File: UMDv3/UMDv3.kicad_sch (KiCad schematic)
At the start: 63 parts

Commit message: version 3.0 gerbers made
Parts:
- C101, C104, C108, C114, C115, C116, C117, C118, C119, C120, C121, C122, C123: value (none) -> 0.1uF/50V; footprint (none) -> db-smt:0603
- C102, C103, C107: value (none) -> 10uF/25V; footprint (none) -> db-smt:0805
- C105, C106: value (none) -> 2.2uF/16V; footprint (none) -> db-smt:0805
- C109, C110: value (none) -> 22pF/50V; footprint (none) -> db-smt:0603
- C111, C112, C113: value (none) -> 1uF/16V; footprint (none) -> db-smt:0805
- CON101, CON102: value (none) -> 10118192-0002LF; footprint (none) -> db-smt:USB-10118192-0002
- CON103, CON107: value (none) -> HDR1X3; footprint (none) -> db-thparts:HDR1X3
- CON104: value (none) -> JTAG-2X10-HDR; footprint (none) -> db-thparts:HDR2X10-JTAG-SHROUD
- CON105: value (none) -> 101-00405-75; footprint (none) -> db-smt:SDCARD-AMP-10100405
- CON106: value (none) -> UMDv3-CONN; footprint (none) -> db-thparts:UMDv3-CONN-DIP64-2
- D101, D102: value (none) -> LO_M67K-K2M1-24-Z; footprint (none) -> db-smt:SMD-2
- D103, D104: value (none) -> LG_M67K-G1J2-24-Z; footprint (none) -> db-smt:SMD-2
- FB101: value (none) -> 1K@100MHz; footprint (none) -> db-smt:0805
- MEC101, MEC102, MEC103, MEC104: value (none) -> NSP-4-6-01; footprint (none) -> db-thparts:4-40-SCREW
- R101: value (none) -> 1.5k; footprint (none) -> db-smt:0603
- R102, R103: value (none) -> 2.2k; footprint (none) -> db-smt:0603
- R104, R105, R106, R108, R110: value (none) -> 470; footprint (none) -> db-smt:0603
- R107, R111: value (none) -> 10k; footprint (none) -> db-smt:0603
- R109: value (none) -> 715; footprint (none) -> db-smt:0603
- SW101, SW102, SW103, SW104, SW105, SW106, SW107, SW108: value (none) -> PTS645SM43SMTR92_LFS; footprint (none) -> db-smt:PTS645
- U101: value (none) -> MCP23008T-E_SO; footprint (none) -> db-smt:SOIC-18
- U102: value (none) -> AZ1117CH-3.3TRG1; footprint (none) -> db-smt:SOT-223
- U103: value (none) -> STM32F407VET6TR; footprint (none) -> db-smt:TQFP-100
- U104: value (none) -> SSD1106-1.3-OLED-I2C; footprint (none) -> db-thparts:OLED-1.3-I2C
- X101: value (none) -> ABLS-8.000MHZ-B4-T; footprint (none) -> db-smt:HC-49US
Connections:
- no-connect marks 0 -> 1

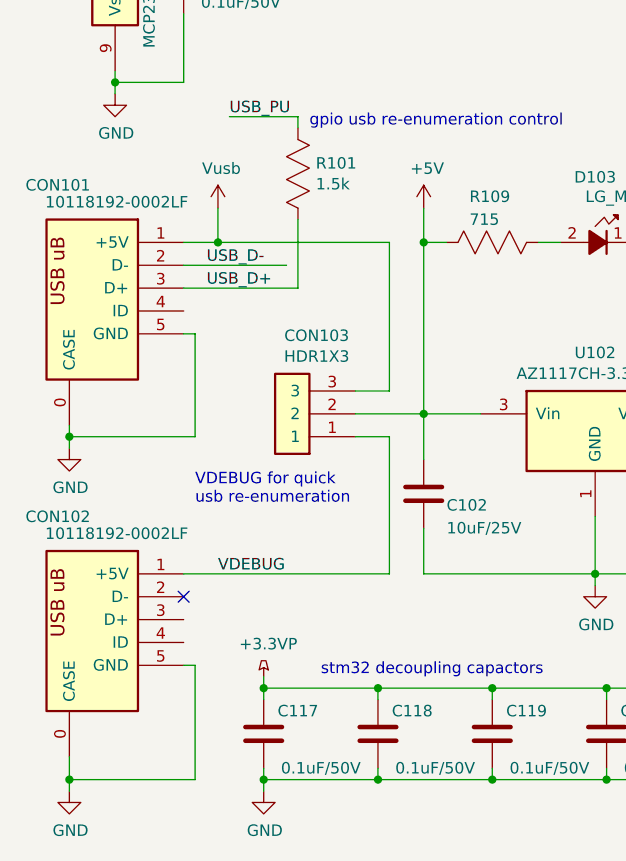
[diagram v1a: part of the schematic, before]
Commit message: updated sch for easier to solder usb conn, no pcb update yet
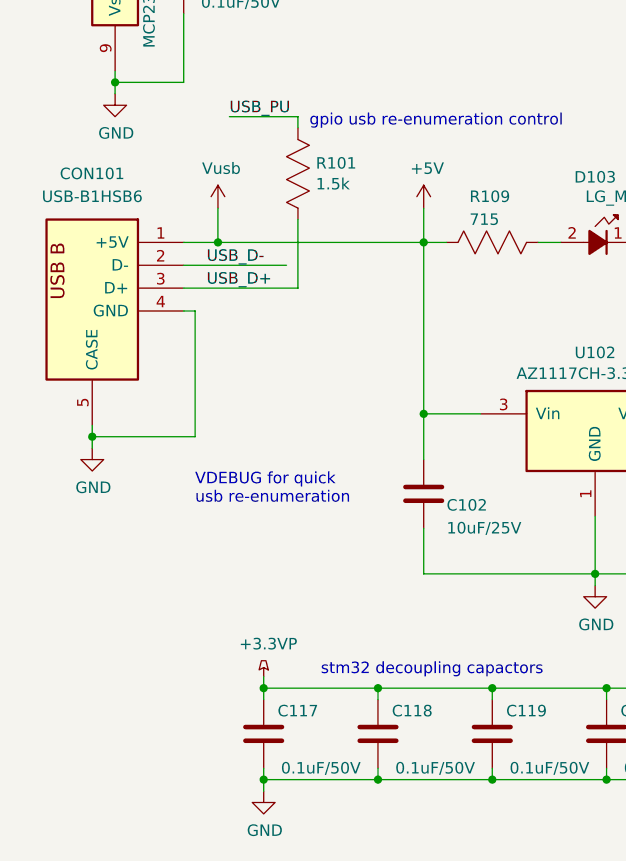
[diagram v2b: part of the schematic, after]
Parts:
- removed CON101, CON102: 10118192-0002LF, db-smt:USB-10118192-0002, symbol db-connectors:10118192-0002LF
- removed CON103: HDR1X3, db-thparts:HDR1X3, symbol db-connectors:HDR1X3
- added CON101: USB-B1HSB6, db-thparts:USB-B1HSxx, symbol db-connectors:USB-B1HSB6
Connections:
- net +5V: now also CON101.1 (+5V)
- net GND: now also CON101.4 (GND), CON101.5 (CASE)
- net USB_D+: now also CON101.3 (D+)
- net USB_D-: now also CON101.2 (D-)
- no-connect marks 1 -> 0

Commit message: work
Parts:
- removed U101: MCP23008T-E_SO, db-smt:SOIC-18, symbol db-sem:MCP23008T-E_SO
- added TP101: TP_2.25x3_ROUNDED, db-smt:TP_2.25x3_RND, symbol db-connectors:TP_2.25x3_ROUNDED
- added U101: MCP23008T-E_SS, db-smt:SSOP-20, symbol db-sem:MCP23008T-E_SS
- added logo101: db-logo, db-artwork:db-logo_10mm, symbol db-artwork:logo
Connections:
- net +3V3: now also U101.20 (Vdd), U101.3 (A2), U101.4 (A1), U101.5 (A0), U101.6 (~{RESET})
- net BACK: now also U101.17 (GP5)
- net DOWN: now also U101.13 (GP1)
- net GND: now also TP101.1, U101.9 (Vss)
- net LEFT: now also U101.12 (GP0)
- net MCP_INT: now also U101.8 (INT)
- net OK: now also U101.16 (GP4)
- net RIGHT: now also U101.15 (GP3)
- net SCL: now also U101.1 (SCL)
- net SDA: now also U101.2 (SDA)
- net UP: now also U101.14 (GP2)
- net at R105.2: now also U101.18 (GP6)
- net at R106.1: now also U101.19 (GP7)
- no-connect marks 0 -> 2
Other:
- note added: "i2c addr 0x27"
- note removed: "VDEBUG for quick usb re-enumeration"
- moved on the sheet: C115

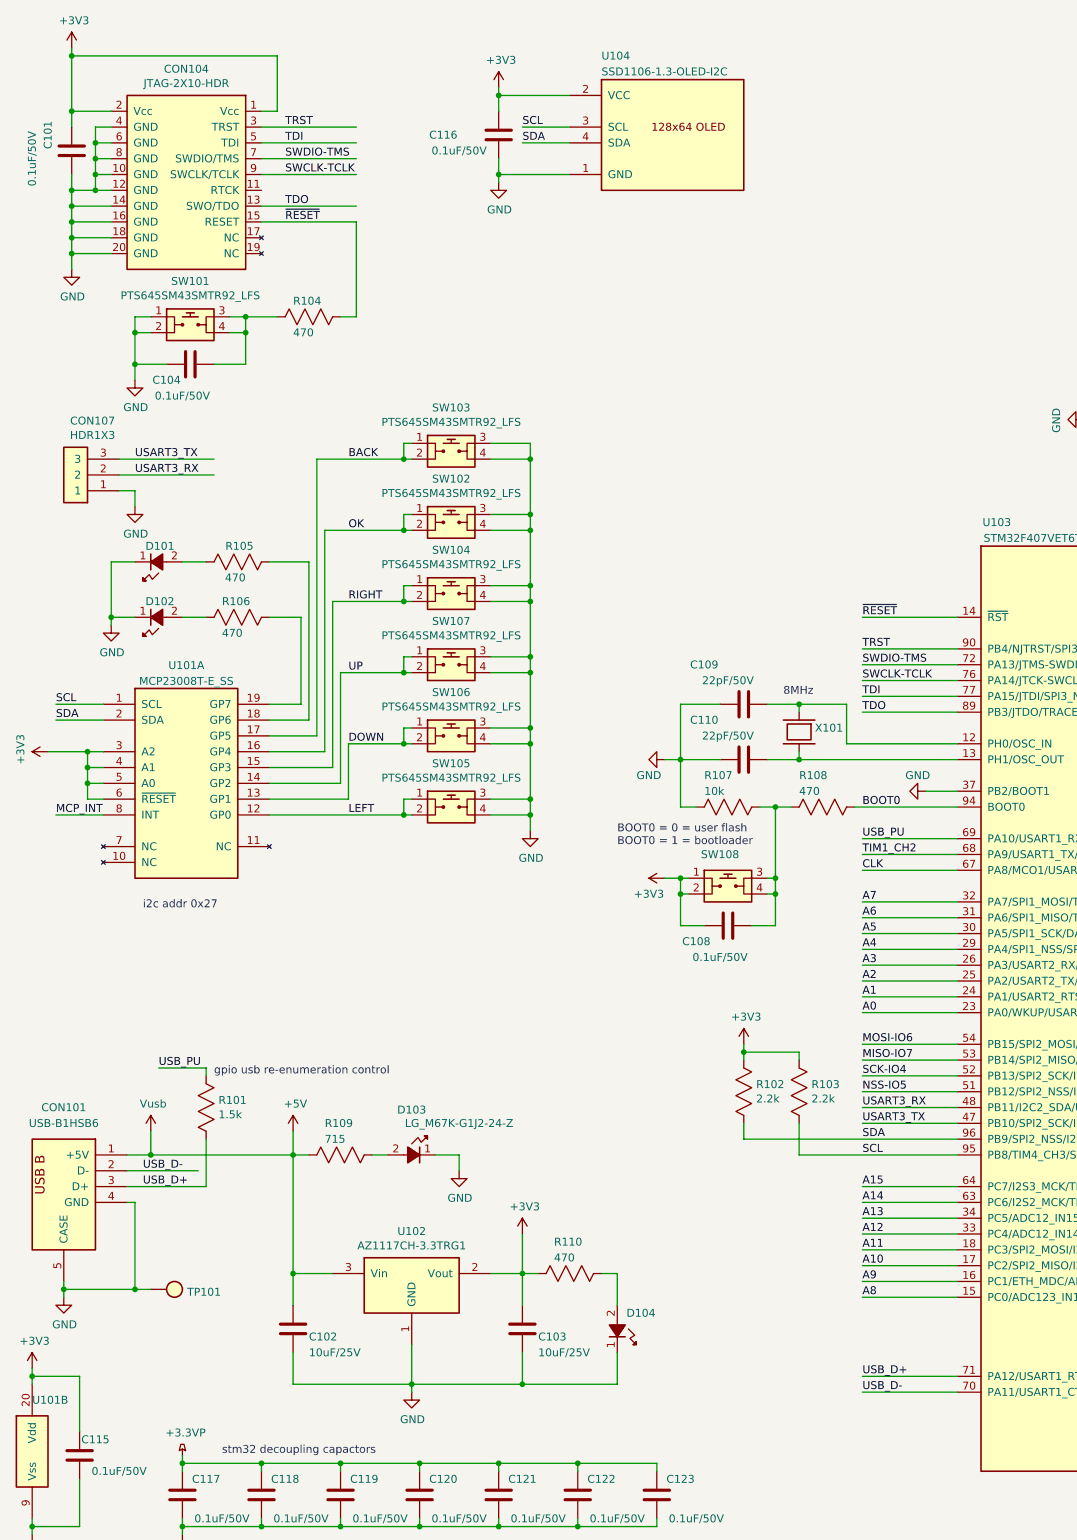
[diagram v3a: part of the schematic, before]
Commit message: changed leds to 3mm, usb conn to th type b
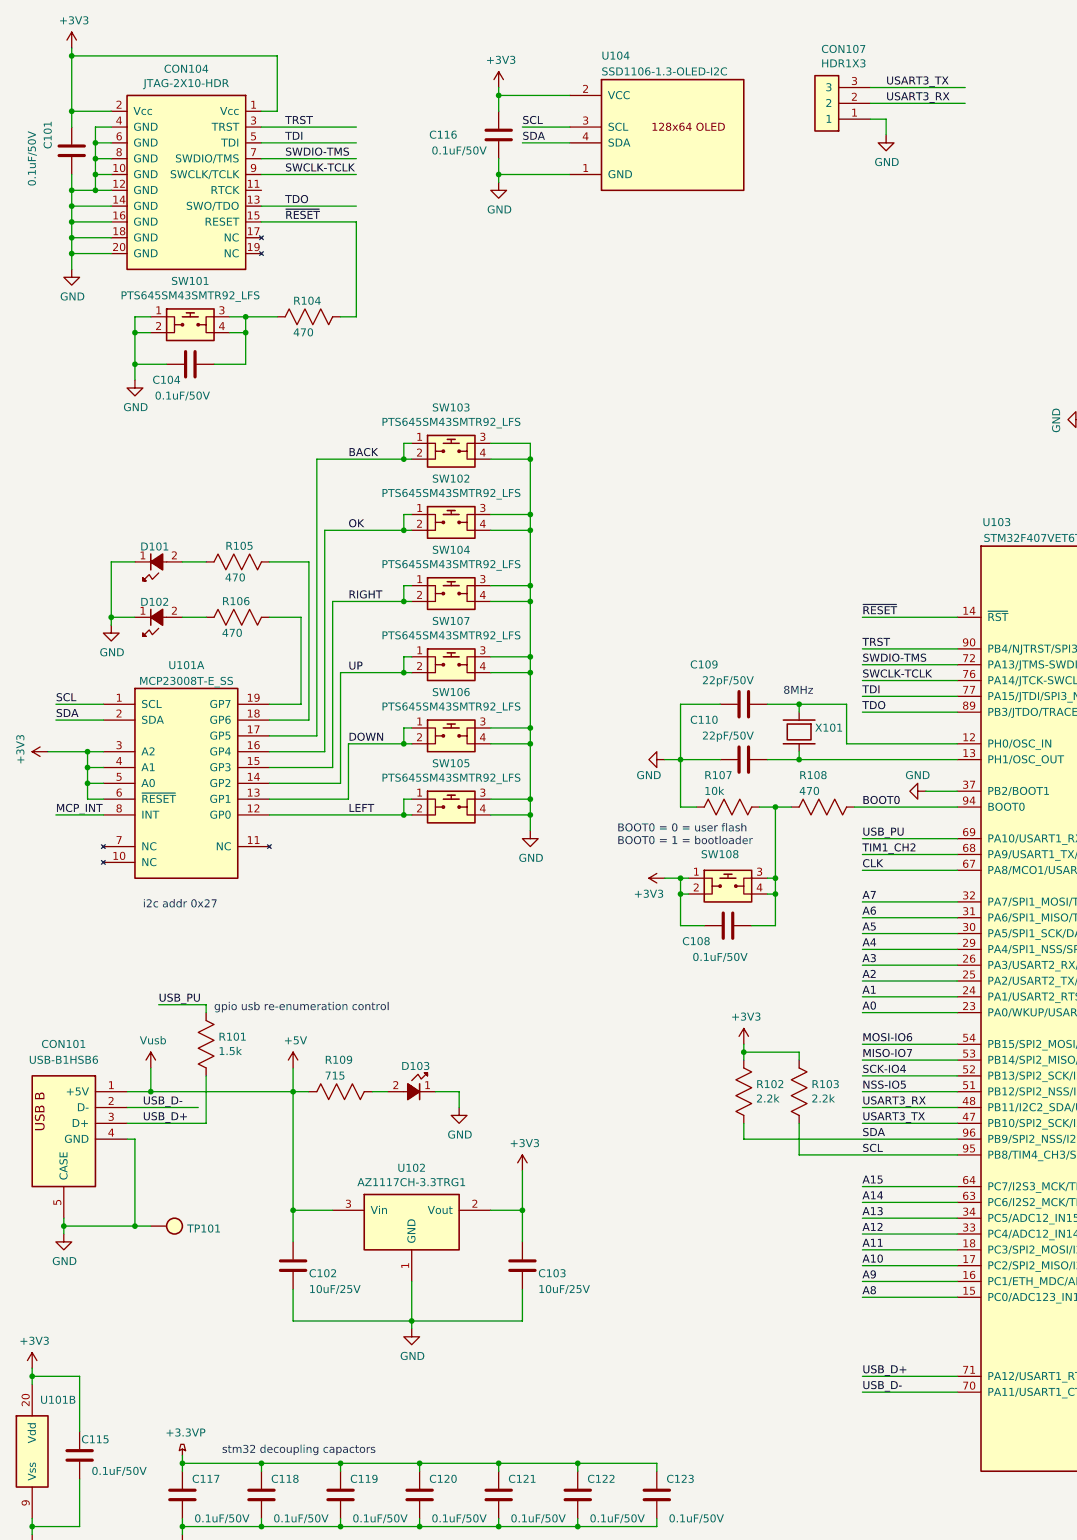
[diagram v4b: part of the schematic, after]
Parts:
- removed D101, D102: LO_M67K-K2M1-24-Z, db-smt:SMD-2, symbol db-diodes:LO_M67K-K2M1-24-Z
- removed D103, D104: LG_M67K-G1J2-24-Z, db-smt:SMD-2, symbol db-diodes:LG_M67K-G1J2-24-Z
- removed R110: 470, db-smt:0603, symbol db-passives:R_0603
- added D101, D102: 151031VS06000, db-thparts:LED-3MM, symbol db-diodes:151031VS06000
- added D103: 151033RS03000, db-thparts:LED-3MM, symbol db-diodes:151033RS03000
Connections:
- net GND: now also D101.1, D102.1, D103.1
- net at R105.1: now also D101.2
- net at R109.1: now also D103.2
- net at R106.2: now also D102.2
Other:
- moved on the sheet: C102, C103, CON101, CON107, R101, R109, TP101, U102
